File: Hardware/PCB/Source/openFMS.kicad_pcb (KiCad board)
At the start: 2 copper layers, 39 parts, among them U1 STM32F030F4Px, U4 ITR9608-F

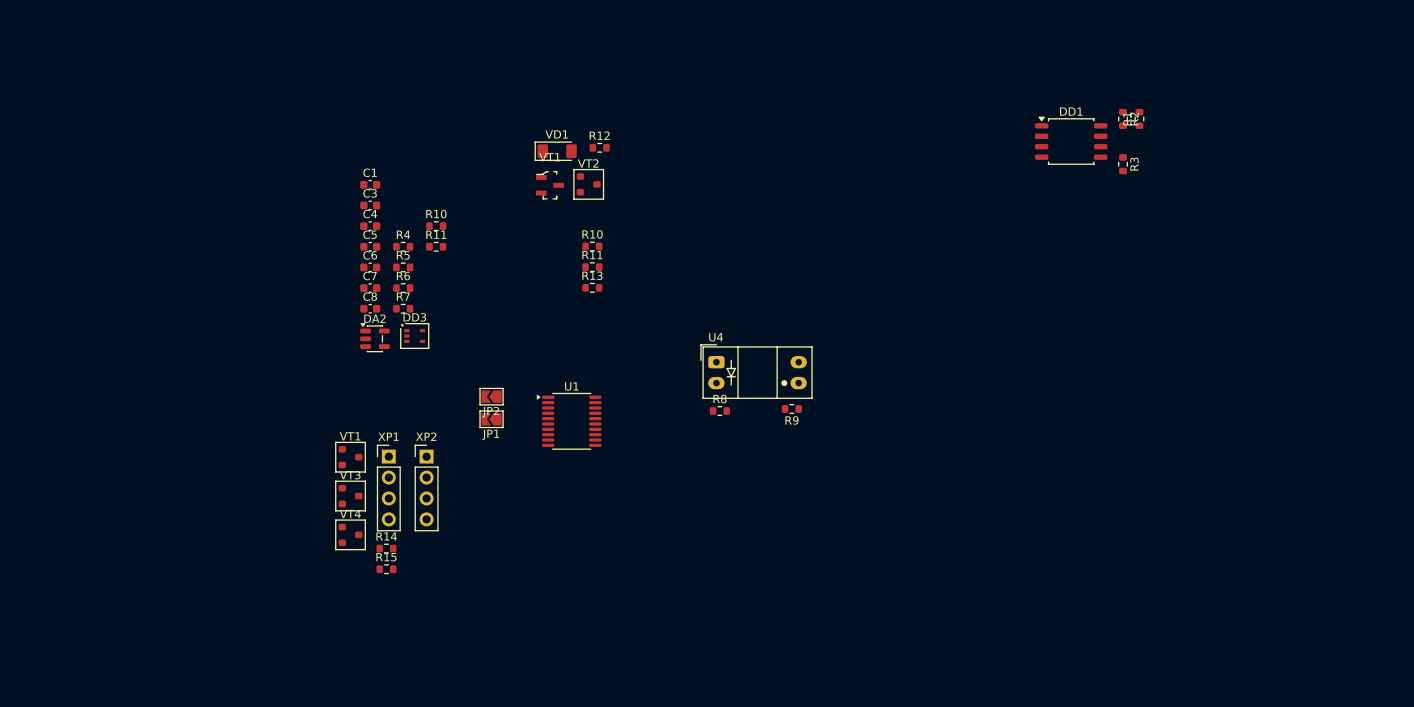
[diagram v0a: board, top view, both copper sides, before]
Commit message: Add input protection for comparator, spare connector, update crystal load caps
Added Schottky diodes (BAT54CW) and current‑limiting resistors (10 kΩ) to protect MCP6541 comparator inputs from overvoltage/ESD. Introduced a spare connector wired to unused microcontroller GPIOs for future expansion. Updated crystal resonator (DSX321G‑8MHz‑12pF) load capacitors to recommended values (e.g., 15–18 pF) for stable oscillation.
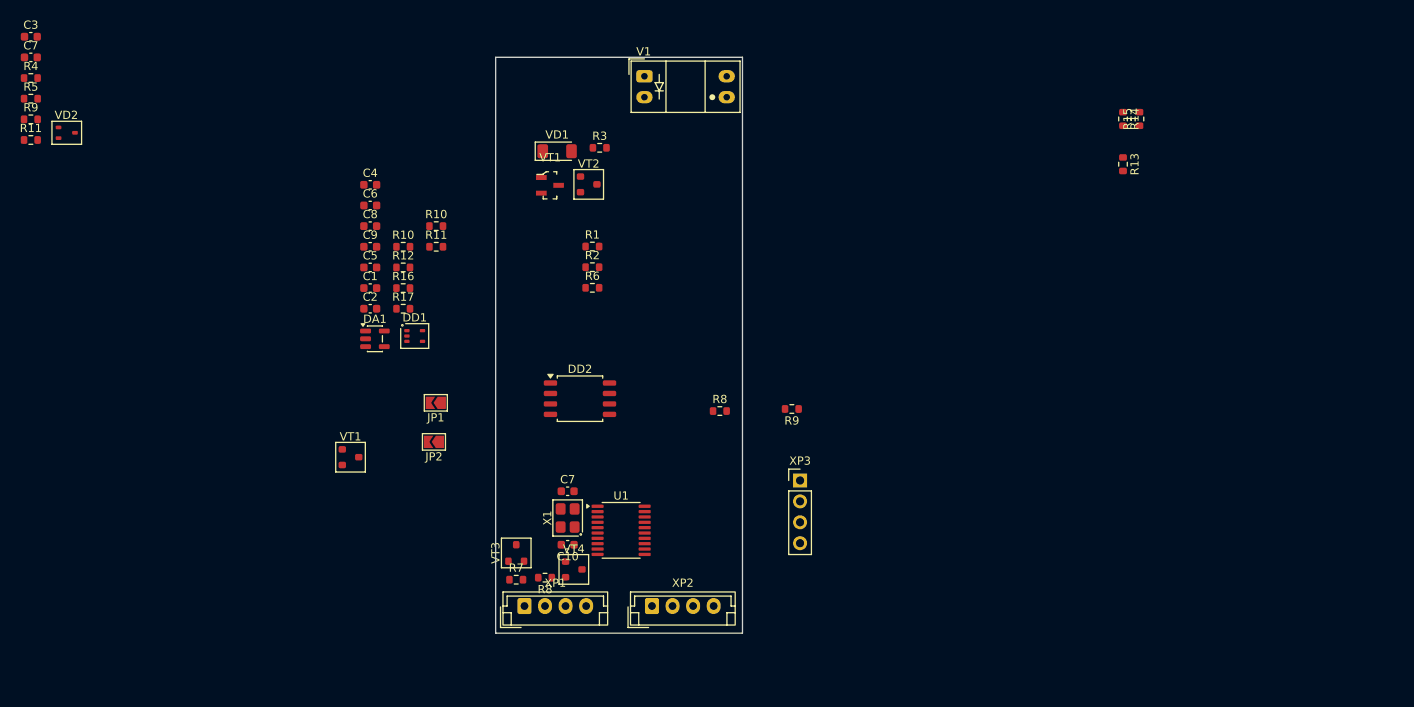
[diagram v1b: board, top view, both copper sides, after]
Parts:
- added C10: 18 pF, Capacitor_SMD:C_0603_1608Metric, F.Cu at (125.2, 106.2)
- added C3: 4.7 uF, Capacitor_SMD:C_0603_1608Metric, F.Cu at (60.0, 44.5)
- added C7: 18 pF, Capacitor_SMD:C_0603_1608Metric, F.Cu at (125.2, 99.8)
- added C7: 4.7 uF, Capacitor_SMD:C_0603_1608Metric, F.Cu at (60.0, 47.0)
- added R11: 10k, Resistor_SMD:R_0603_1608Metric, F.Cu at (60.0, 57.1)
- added R4: 10k, Resistor_SMD:R_0603_1608Metric, F.Cu at (60.0, 49.5)
- added R5: 10k, Resistor_SMD:R_0603_1608Metric, F.Cu at (60.0, 52.0)
- added R9: 110, Resistor_SMD:R_0603_1608Metric, F.Cu at (60.0, 54.5)
- added VD2: BAT54CW, Package_TO_SOT_SMD_AKL:SOT-323_SC-70, F.Cu at (64.4, 56.2)
- added X1: 8 MHz, Crystal_AKL:Crystal_SMD_3225-4Pin_3.2x2.5mm, F.Cu at (125.2, 103.0)
- added XP2: Conn_01x04, Connector_JST:JST_EH_B4B-EH-A_1x04_P2.50mm_Vertical, F.Cu at (135.5, 113.7)
- XP1: footprint Connector_PinHeader_2.54mm:PinHeader_1x04_P2.54mm_Vertical -> Connector_JST:JST_EH_B4B-EH-A_1x04_P2.50mm_Vertical
- moved DD2 67.4 mm to (126.8, 88.5)
- moved XP3 45.5 mm to (153.5, 98.4)
- moved V1 35.8 mm to (134.6, 49.3)
- moved VT4 27.5 mm to (126.0, 109.2)
- moved XP1 24.5 mm to (120.0, 113.7)
- moved VT3 21.3 mm to (119.0, 107.2), turned to 90 degrees
- moved R8 19.3 mm to (122.5, 110.2), turned to 180 degrees
- moved R7 16.2 mm to (119.0, 110.5)
- moved U1 14.5 mm to (131.8, 104.5)
- moved JP2 8.90 mm to (109.0, 93.8)
- moved JP1 7.06 mm to (109.2, 89.0)
- renumbered C7 to C1, C8 to C2, C1 to C4, C6 to C5, C3 to C6, C4 to C8, C5 to C9, DA2 to DA1, DD3 to DD1, DD1 to DD2, R10 to R1, R4 to R10, R5 to R12, R3 to R13, R2 to R14, R1 to R15, R6 to R16, R7 to R17, R11 to R2, R12 to R3, R13 to R6, R14 to R7, R15 to R8, U4 to V1, XP2 to XP3
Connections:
- DA1 pad 3: Net-(DA2-EN) -> Net-(DA1-EN)
- DD1 pad 4: Net-(DD3--) -> Net-(DD1--)
- R1 pad 2: Net-(DD3--) -> Net-(R1-Pad2)
- R2 pad 1: Net-(DD3--) -> Net-(R1-Pad2)
- R3 pad 2: /2V_REF -> Net-(VD1-K)
- R6 pad 2: Net-(DA2-EN) -> Net-(DA1-EN)
- U1 pad 10: unconnected-(U1-PA4-Pad10) -> /PA4
- U1 pad 11: unconnected-(U1-PA5-Pad11) -> /PA5
- U1 pad 2: unconnected-(U1-PF0-Pad2) -> Net-(U1-PF0)
- U1 pad 3: unconnected-(U1-PF1-Pad3) -> Net-(U1-PF1)
- V1 pad 1: +3V3 -> Net-(R9-Pad2)
- V1 pad 2: Net-(R8-Pad1) -> GND
- VD1 pad 1: /2V_REF -> Net-(VD1-K)
- VT1 pad 3: Net-(DA2-EN) -> Net-(DA1-EN)
- VT2 pad 1: Net-(DA2-EN) -> Net-(DA1-EN)
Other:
- board outline added: 30 x 70 mm

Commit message: Edit PCB
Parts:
- removed the C3 at (60.0, 44.5)
- removed the C7 at (60.0, 47.0)
- removed the VT1 at (123.1, 62.6)
- R8: value 110 -> 10k
- moved R12 119.6 mm to (224.3, 84.2)
- moved JP2 112.3 mm to (220.8, 84.2)
- moved R10 105.9 mm to (210.0, 85.2)
- moved JP1 104.3 mm to (213.5, 85.2)
- moved C3 90.9 mm to (215.8, 91.5)
- moved C7 90.9 mm to (215.8, 98.0)
- moved X1 90.9 mm to (215.8, 94.8)
- moved U1 90.7 mm to (222.1, 97.5)
- moved R5 79.6 mm to (120.5, 103.8), turned to 90 degrees
- moved R4 77.3 mm to (120.8, 97.2)
- moved VD2 72.4 mm to (125.0, 95.8), turned to 90 degrees
- moved C5 68.0 mm to (169.2, 72.0), turned to -90 degrees
- moved R7 52.5 mm to (170.8, 101.5)
- moved R8 52.5 mm to (174.2, 101.2)
- moved VT3 52.5 mm to (170.8, 98.2)
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- renumbered C7 to C3, C10 to C7
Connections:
- R8 pad 1: Net-(R8-Pad1) -> /FILAMENT_SENS

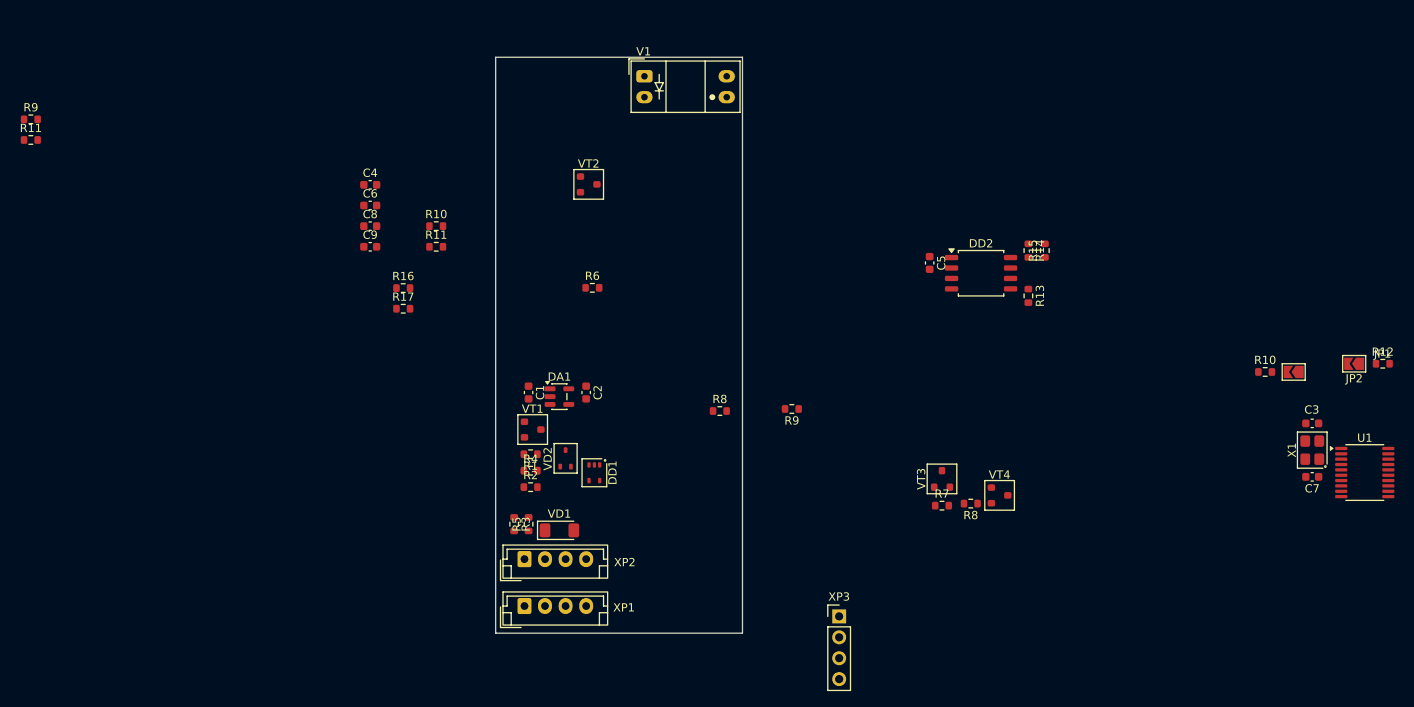
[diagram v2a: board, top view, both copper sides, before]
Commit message: WIP: PCB component placement draft + FreeCAD 3D models
Finished rough component placement on PCB (routing not started). Added draft FreeCAD models for PCB and filament rod to visualize mechanical compatibility.
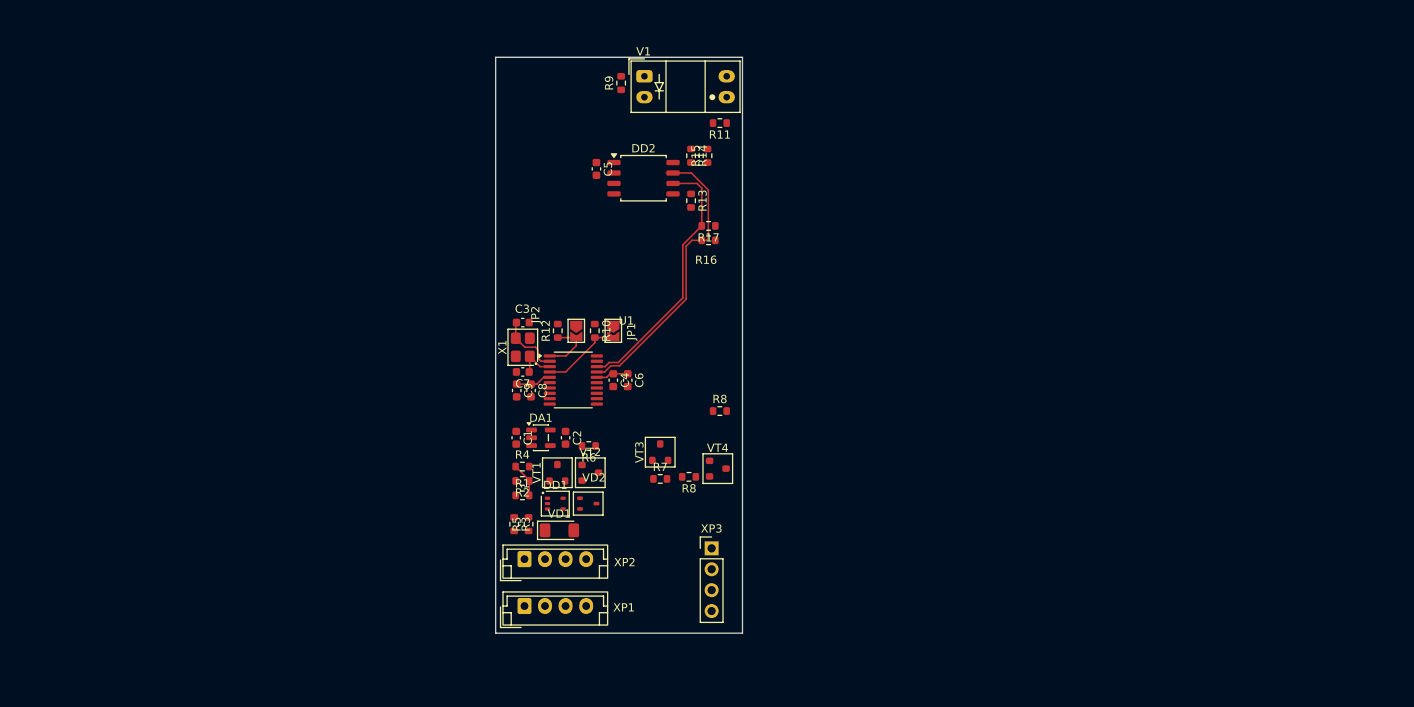
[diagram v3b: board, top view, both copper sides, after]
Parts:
- removed the R10 at (109.3, 67.5)
- removed the R11 at (109.3, 70.0)
- removed the R11 at (60.0, 57.1)
- removed the R9 at (60.0, 54.5)
- added R11: 10k, Resistor_SMD:R_0603_1608Metric, F.Cu at (143.8, 55.0)
- R9: value 10k -> 110
- moved R12 100.4 mm to (124.0, 80.2), turned to 90 degrees
- moved U1 96.9 mm to (125.9, 86.2)
- moved C7 96.8 mm to (119.8, 85.2)
- moved X1 96.8 mm to (119.8, 82.2)
- moved C3 96.7 mm to (119.8, 79.2)
- moved JP2 94.6 mm to (126.3, 80.2), turned to -90 degrees
- moved JP1 82.9 mm to (130.8, 80.2), turned to -90 degrees
- moved R10 81.6 mm to (128.6, 80.2), turned to -90 degrees
- moved R9 44.7 mm to (131.8, 50.1), turned to 90 degrees
- moved DD2 42.6 mm to (134.5, 61.7)
- moved R13 42.6 mm to (140.2, 64.4)
- moved R14 42.6 mm to (140.2, 59.0)
- moved R15 42.6 mm to (142.2, 59.0)
- moved C5 42.1 mm to (128.8, 60.6)
- moved R17 38.5 mm to (142.4, 67.5), turned to 180 degrees
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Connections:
- JP2 pad 1: /BOOT -> +3V3
- JP2 pad 2: +3V3 -> /BOOT
- R9 pad 1: /PHOTO_OUT -> +3V3
- R9 pad 2: +3V3 -> Net-(R9-Pad2)
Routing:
- net /I2C_SCL: track 0.00 -> 35.9 mm
- net /I2C_SDA: track 0.00 -> 31.9 mm
- net /NRST: track 0.00 -> 9.86 mm
- net +3V3: track 0.00 -> 8.28 mm
- net Net-(U1-PF0): track 0.00 -> 7.80 mm
- net /BOOT: track 0.00 -> 7.11 mm
- net Net-(U1-PF1): track 0.00 -> 4.87 mm
- net Net-(R1-Pad2): track 0.00 -> 4.18 mm

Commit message: WIP: routing
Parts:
- removed the R8 at (140.0, 98.0)
- added R18: 2k, Resistor_SMD:R_0603_1608Metric, F.Cu at (136.0, 86.3)
- added R19: 2k, Resistor_SMD:R_0603_1608Metric, F.Cu at (134.2, 86.3)
- added VT5: BSS138L, Package_TO_SOT_SMD_AKL:SOT-23, F.Cu at (133.0, 112.8)
- added VT6: BSS138L, Package_TO_SOT_SMD_AKL:SOT-23, F.Cu at (133.0, 107.2)
- R11: value 10k -> 110
- R16, R17: value 2k -> 10k
- R9: value 110 -> 10k
- moved R9 65.4 mm to (132.8, 115.5), turned to 0 degrees
- moved R10 30.0 mm to (132.8, 109.9), turned to 0 degrees
- moved R14 26.8 mm to (124.0, 80.2), turned to 90 degrees
- moved XP3 25.4 mm to (139.8, 81.4)
- moved R8 21.1 mm to (136.8, 109.9)
- moved R11 17.8 mm to (126.8, 60.4), turned to 90 degrees
- moved VT3 17.8 mm to (137.0, 112.8), turned to 0 degrees
- moved R15 17.3 mm to (135.0, 74.7), turned to -90 degrees
- moved R7 17.3 mm to (136.8, 115.5)
- moved VT4 12.1 mm to (137.0, 107.2)
- moved C5 11.4 mm to (123.8, 70.9)
- moved DD2 11.4 mm to (129.5, 72.0)
- moved V1 11.4 mm to (129.6, 59.6)
- moved R16 7.12 mm to (135.2, 69.2), turned to 90 degrees
- moved R17 6.33 mm to (138.5, 72.5), turned to 90 degrees
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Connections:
- R10 pad 1: +3V3 -> /PA4_SIG
- R10 pad 2: /NRST -> GND
- R11 pad 1: /PHOTO_OUT -> +3V3
- R11 pad 2: +3V3 -> Net-(R11-Pad2)
- R12 pad 1: /BOOT -> +3V3
- R12 pad 2: GND -> /NRST
- R13 pad 1: Net-(DD2-PGO) -> /PHOTO_OUT
- R13 pad 2: GND -> +3V3
- R14 pad 1: +3V3 -> /BOOT
- R14 pad 2: Net-(DD2-DIR) -> GND
- R15 pad 1: Net-(DD2-DIR) -> Net-(DD2-PGO)
- R16 pad 2: /I2C_SCL -> Net-(DD2-DIR)
- R17 pad 1: +3V3 -> Net-(DD2-DIR)
- R17 pad 2: /I2C_SDA -> GND
- R8 pad 1: /FILAMENT_SENS -> /PA3_SIG
- R9 pad 1: +3V3 -> /FILAMENT_SENS
- R9 pad 2: Net-(R9-Pad2) -> GND
- U1 pad 11: /PA5 -> unconnected-(U1-PA5-Pad11)
- U1 pad 14: /HALL_OUT -> unconnected-(U1-PB1-Pad14)
- U1 pad 8: unconnected-(U1-PA2-Pad8) -> /HALL_OUT
- U1 pad 9: unconnected-(U1-PA3-Pad9) -> /PA3
- V1 pad 1: Net-(R9-Pad2) -> Net-(R11-Pad2)
- VT4 pad 1: /FILAMENT_SIG -> /PA3
- VT4 pad 2: /FILAMENT_SENS -> /PA3_SIG
- XP2 pad 2: /PA4 -> /PA3_SIG
- XP2 pad 3: /PA5 -> /PA4_SIG
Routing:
- net /FILAMENT_SIG: track 0.00 -> 39.4 mm
- net /MOTION_SIG: track 0.00 -> 36.5 mm
- net /PHOTO_OUT: track 0.00 -> 36.1 mm
- net /HALL_OUT: track 0.00 -> 32.2 mm
- net /PA3_SIG: track 0.00 -> 31.9 mm
- net /PA3: track 0.00 -> 23.8 mm
- net /SWDIO: track 0.00 -> 22.6 mm
- net /SWCLK: track 0.00 -> 22.1 mm
- net /PA4: track 0.00 -> 21.5 mm
- net /PA4_SIG: track 0.00 -> 18.1 mm
- net /MOTION_SENS: track 0.00 -> 17.0 mm
- net Net-(DD1--): track 0.00 -> 11.0 mm
- net /FILAMENT_SENS: track 0.00 -> 10.2 mm
- net Net-(DA1-EN): track 0.00 -> 9.32 mm
- net /I2C_SDA: track 31.9 -> 23.1 mm
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- added copper zone on B.Cu, net GND
- added copper zone on F.Cu, net VCC
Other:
- board size 30 x 70 mm -> 25 x 60 mm

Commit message: WIP: routing
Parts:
- moved R17 3.56 mm to (137.0, 69.3)
- moved R18 1.65 mm to (136.0, 84.7)
- moved R19 1.65 mm to (134.2, 84.7)
- turned R16 to -90 degrees
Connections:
- U1 pad 6: /MOTION_SIG -> /HALL_OUT
- U1 pad 7: /FILAMENT_SIG -> /MOTION_SIG
- U1 pad 8: /HALL_OUT -> /FILAMENT_SIG
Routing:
- net +3V3: track 10.0 -> 73.7 mm, vias 0 -> 10
- net /PA3_SIG: track 31.9 -> 16.7 mm
- net GND: track 0.00 -> 11.6 mm, vias 0 -> 5
- net /PA4_SIG: track 18.1 -> 9.79 mm
- net VCC: track 8.00 -> 0.00 mm
- net /HALL_OUT: track 32.2 -> 24.5 mm
- net /I2C_SCL: track 27.6 -> 23.4 mm
- net Net-(DD2-DIR): track 0.00 -> 3.94 mm
- net Net-(R11-Pad2): track 0.00 -> 2.83 mm
- net /I2C_SDA: track 23.1 -> 20.8 mm
- net Net-(DD2-PGO): track 0.00 -> 1.94 mm
- net /PA4: track 21.5 -> 23.0 mm
- net /PA3: track 23.8 -> 25.2 mm
- net /FILAMENT_SIG: track 39.4 -> 38.6 mm
- net /FILAMENT_SENS: track 10.2 -> 9.55 mm
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- added copper zone on B.Cu, net +3V3
- added copper zone on F.Cu, net GND

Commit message: WIP: routing and mechanical development
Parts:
- added REF**: MountingHole_3.2mm_M3_DIN965, MountingHole:MountingHole_3.2mm_M3_DIN965, F.Cu at (119.8, 60.2)
- added REF**: MountingHole_2.2mm_M2, MountingHole:MountingHole_2.2mm_M2, F.Cu at (119.5, 95.4)
- added REF**: MountingHole_3.2mm_M3_DIN965, MountingHole:MountingHole_3.2mm_M3_DIN965, F.Cu at (138.2, 113.8)
- moved R1 8.73 mm to (128.2, 102.2), turned to 180 degrees
- moved XP1 7.70 mm to (119.8, 106.0), turned to -90 degrees
- moved R7 7.50 mm to (129.3, 115.5)
- moved R8 7.50 mm to (129.3, 109.9)
- moved VT3 7.50 mm to (129.5, 112.8)
- moved VT4 7.50 mm to (129.5, 107.2)
- moved VD1 7.45 mm to (118.1, 100.3), turned to -90 degrees
- moved R4 7.43 mm to (124.8, 102.2)
- moved R3 5.38 mm to (120.8, 98.7), turned to 180 degrees
- moved XP2 5.11 mm to (124.7, 106.0), turned to -90 degrees
- moved R2 4.14 mm to (121.5, 102.2)
- moved R5 3.24 mm to (120.8, 100.5), turned to 0 degrees
- moved C1 1.77 mm to (118.8, 91.5)
- moved C2 1.77 mm to (124.8, 91.5)
- moved DA1 1.77 mm to (121.8, 91.5)
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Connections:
- U1 pad 10: /PA4 -> /PA3
- U1 pad 7: /MOTION_SIG -> /FILAMENT_SIG
- U1 pad 8: /FILAMENT_SIG -> /MOTION_SIG
- U1 pad 9: /PA3 -> /PA4
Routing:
- net +3V3: track 73.7 -> 56.1 mm, vias 10 -> 7
- net /PA3_SIG: track 16.7 -> 6.18 mm
- net GND: track 11.6 -> 2.20 mm, vias 5 -> 0
- net /FILAMENT_SENS: track 9.55 -> 18.8 mm
- net /2V_REF: track 7.35 -> 14.2 mm
- net Net-(DD1--): track 11.4 -> 5.19 mm
- net /FILAMENT_SIG: track 38.6 -> 34.5 mm
- net /PA3: track 25.2 -> 23.3 mm
- net Net-(R1-Pad2): track 4.18 -> 5.82 mm
- net Net-(VD1-K): track 3.75 -> 5.38 mm
- net /MOTION_SIG: track 36.2 -> 37.2 mm
- net /PA4: track 23.0 -> 23.8 mm
- net /MOTION_SENS: track 16.7 -> 16.1 mm
